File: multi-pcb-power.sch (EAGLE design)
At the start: 17 parts, among them Q5 TIP136, T2 BC618

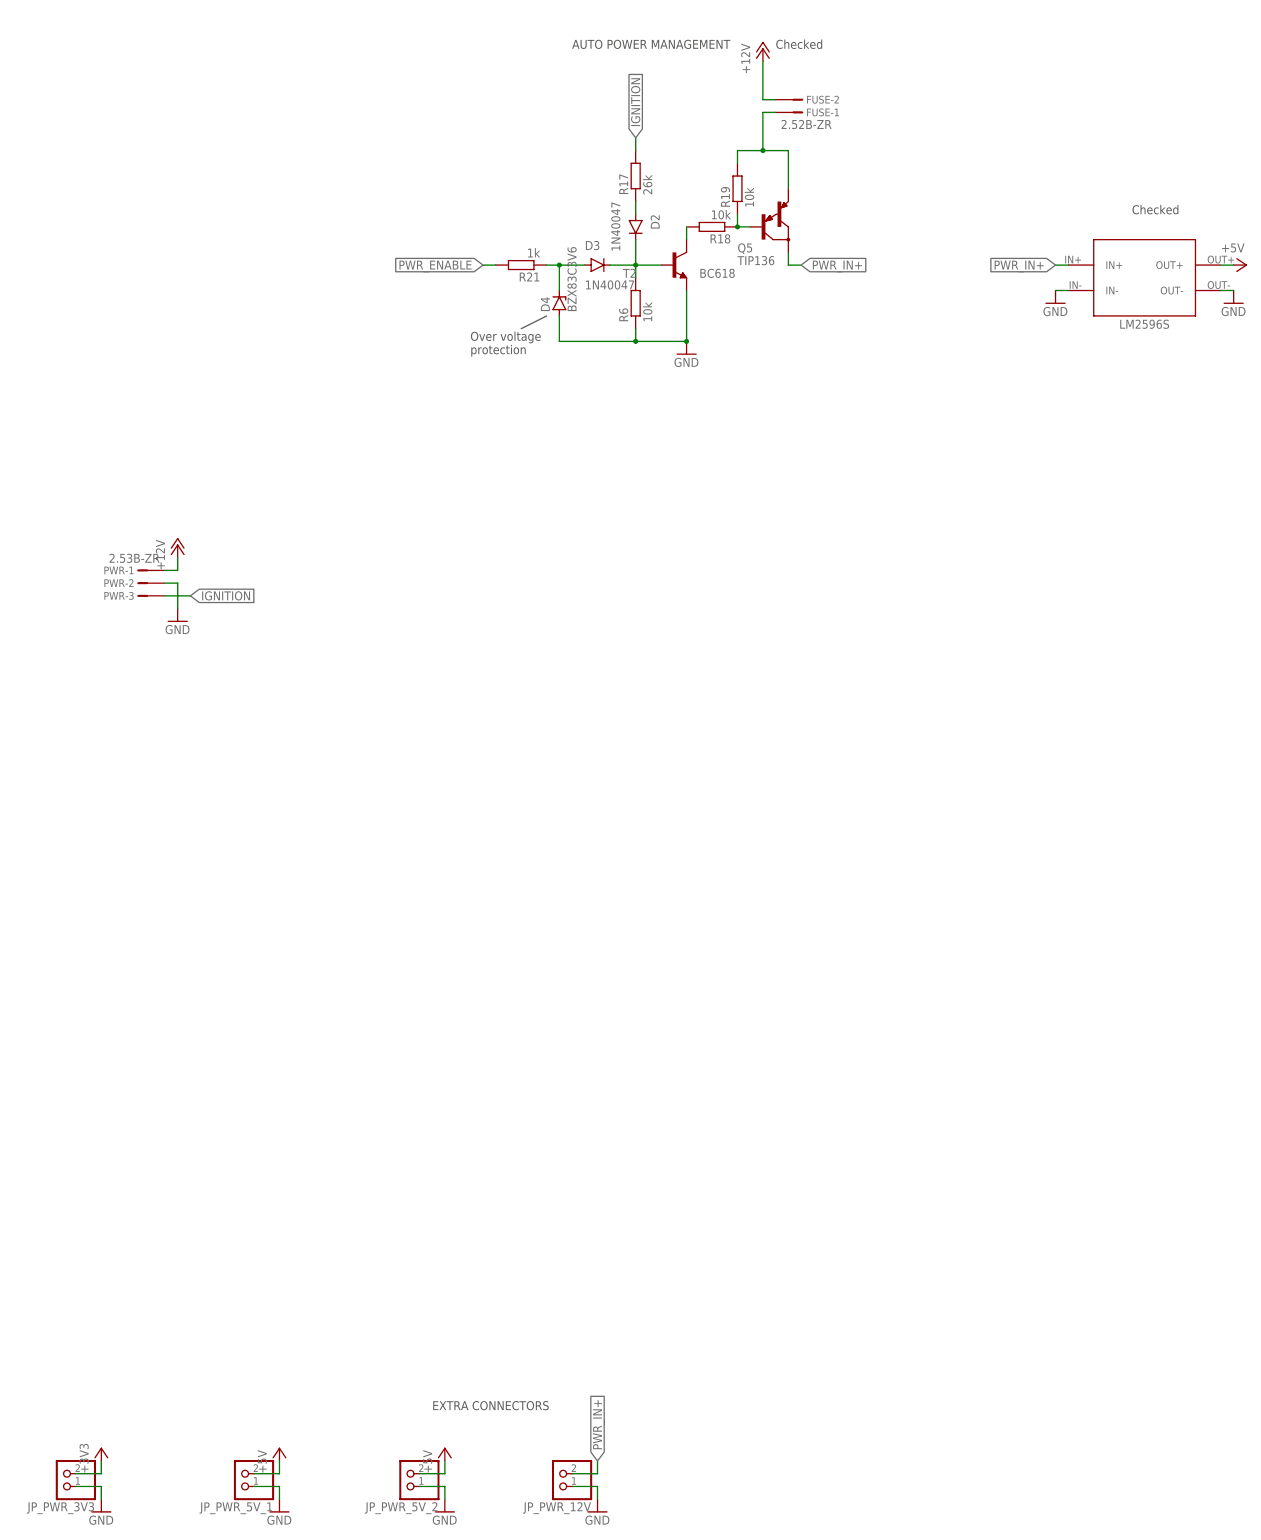
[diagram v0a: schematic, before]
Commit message: Routed more multi-pcb boards
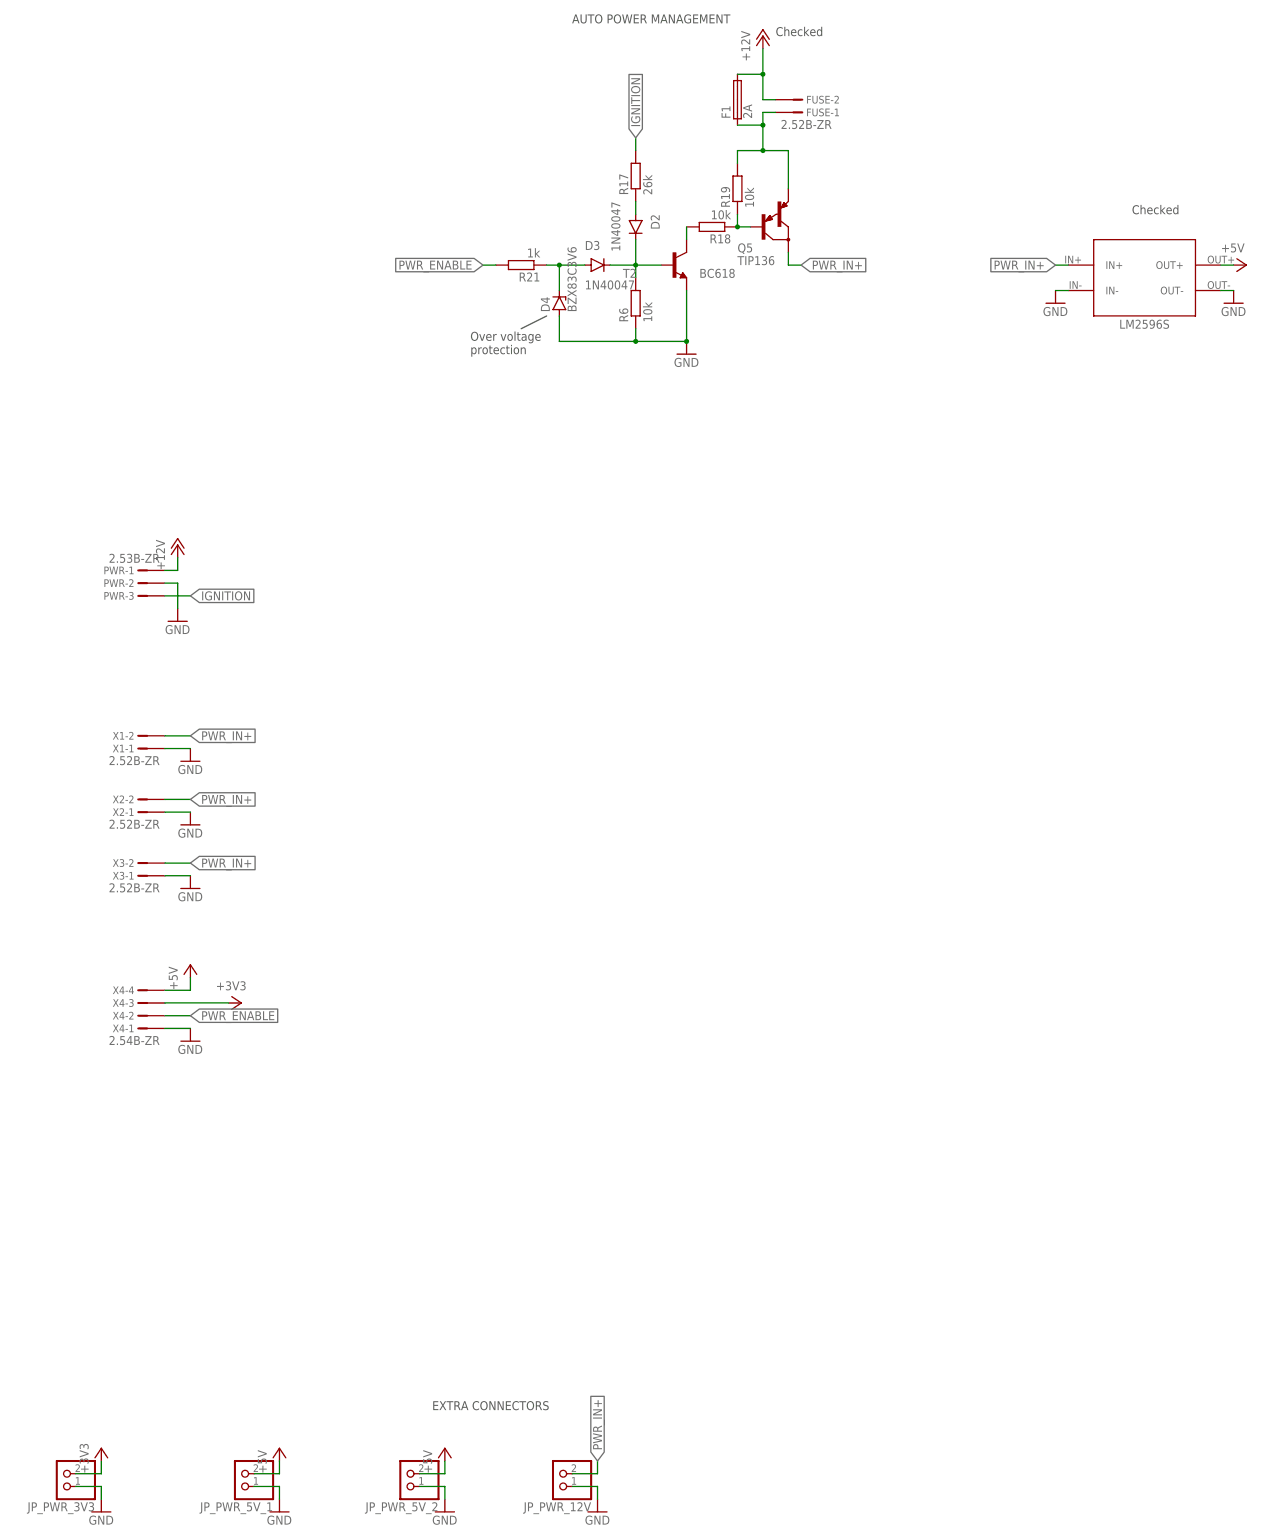
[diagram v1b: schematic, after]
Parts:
- added F1: 2A, fuse:SHK20L
- added X1, X2, X3: 2.52B-ZR, con-jst-custom:2.52B-ZR
- added X4: 2.54B-ZR, con-jst-custom:2.54B-ZR
- R17, R19: device rcl:R-EU_0207/7 -> rcl:R-EU_0207/10
- R21: device rcl:R-EU_0309/10 -> rcl:R-EU_0207/10
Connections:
- net +12V: now also F1.2A
- net +3V3: now also X4-3.1
- net +5V: now also X4-4.1
- net GND: now also X1-1.1, X2-1.1, X3-1.1, X4-1.1
- net N$21: now also F1.1A
- net PWR_ENABLE: now also X4-2.1
- net PWR_IN+: now also X1-2.1, X2-2.1, X3-2.1

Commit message: Made schematic more compact/clean
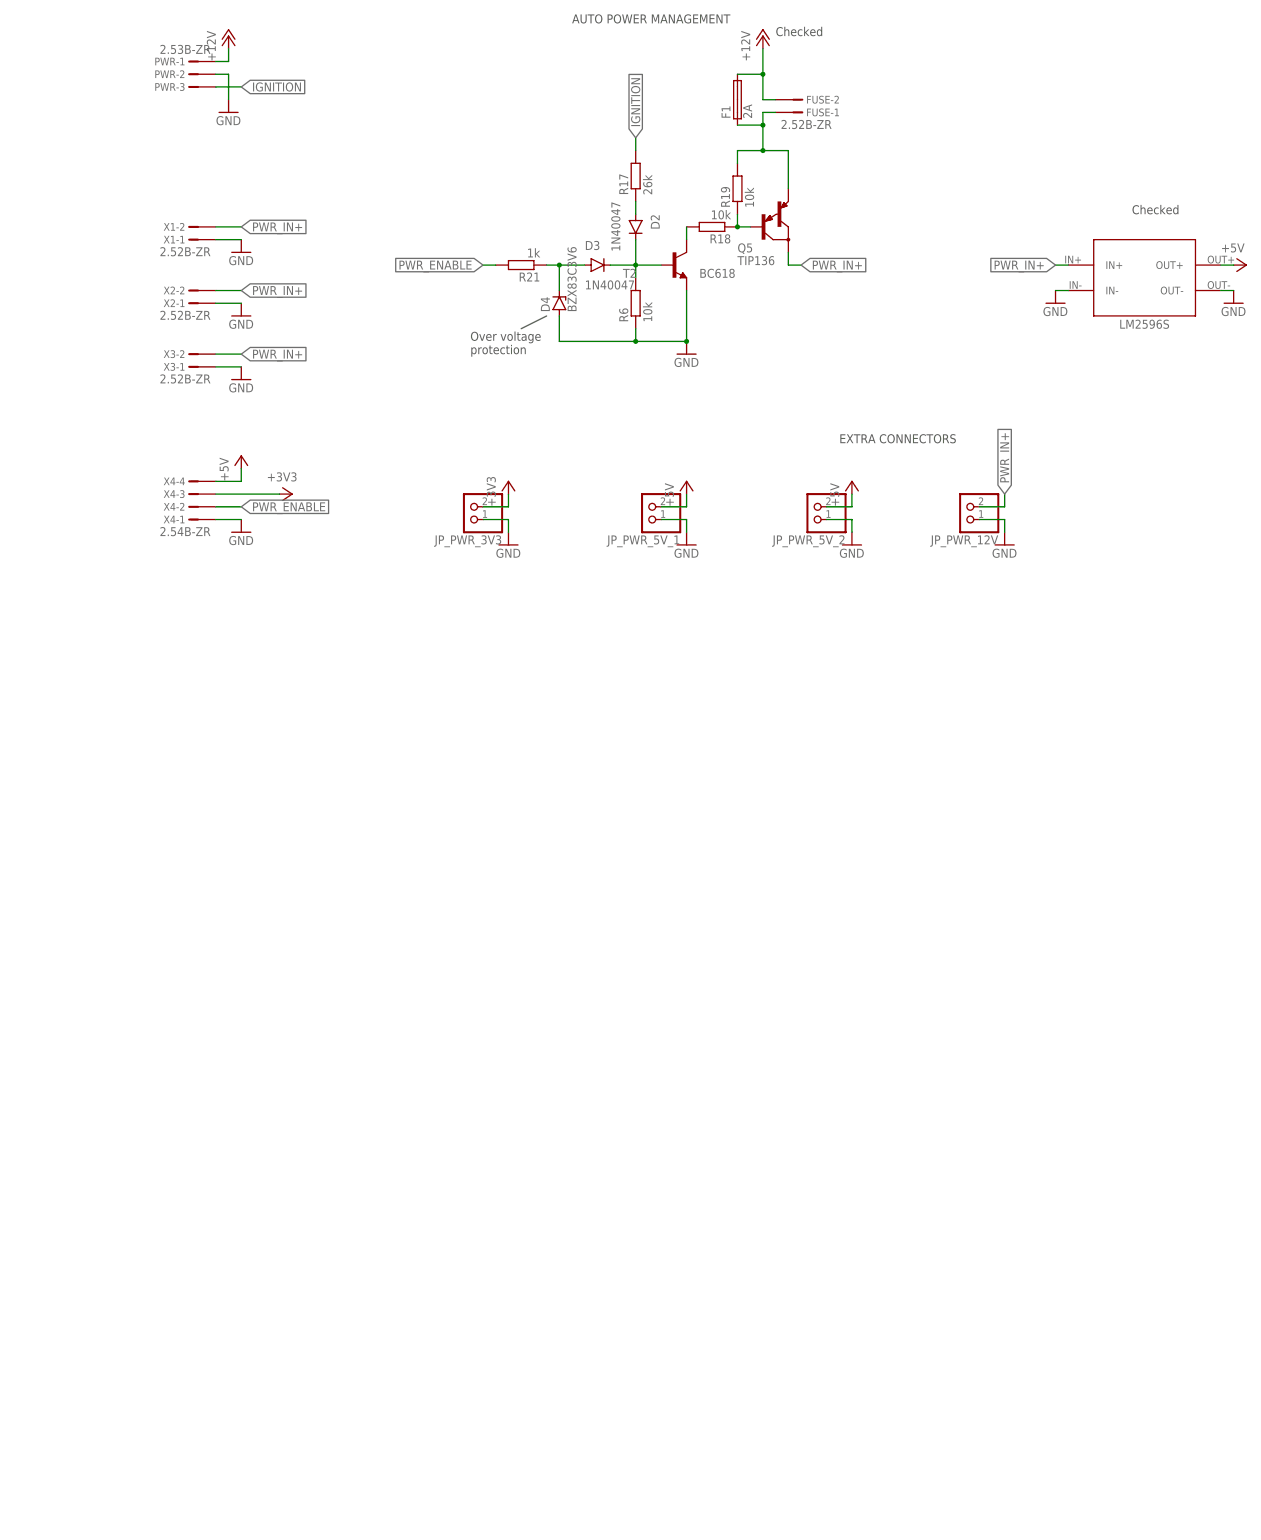
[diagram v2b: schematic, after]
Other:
- moved on the sheet: JP_PWR_12V, JP_PWR_3V3, JP_PWR_5V_1, JP_PWR_5V_2, PWR-1, PWR-2, PWR-3, X1-1, X1-2, X2-1, X2-2, X3-1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
